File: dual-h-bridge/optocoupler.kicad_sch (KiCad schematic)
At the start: 5 parts, among them U2 MCT6

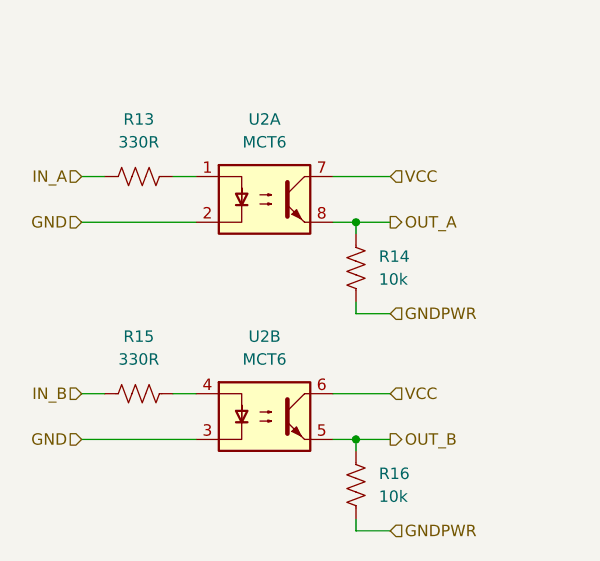
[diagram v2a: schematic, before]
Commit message: Fix optocoupler hardware issue
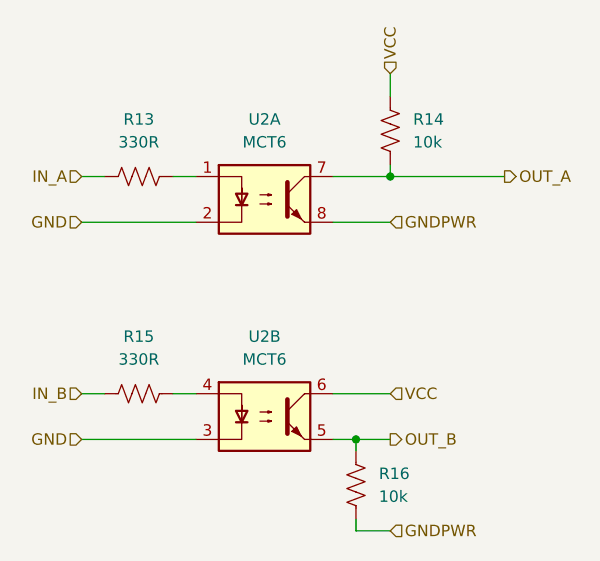
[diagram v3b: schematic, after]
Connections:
- net GNDPWR: now also U2.8; no longer R14.1
- net OUT_A: now also R14.1, U2.7; no longer R14.2, U2.8
- net VCC: now also R14.2; no longer U2.7
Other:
- moved on the sheet: R14
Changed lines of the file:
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@@
 	(title_block
 		(title "Optocoupler")
-		(date "2025-07-06")
-		(rev "v2.0.1")
+		(date "2025-07-09")
+		(rev "v3.0.0")
 		(company "Team 5")
 		(comment 1 "George Sleen")
 	)
 	(junction
-		(at 115.57 54.61)
+		(at 119.38 49.53)
 		(diameter 0)
 		(color 0 0 0 0)
@@
 	(wire
 		(pts
-			(xy 115.57 54.61) (xy 113.03 54.61)
+			(xy 113.03 54.61) (xy 119.38 54.61)
 		)
 		(stroke
@@
 	(wire
 		(pts
-			(xy 115.57 63.5) (xy 115.57 64.77)
-		)
-		(stroke
-			(width 0)
-			(type default)
-		)
-	)
-	(wire
-		(pts
 			(xy 115.57 78.74) (xy 113.03 78.74)
 		)
@@
 	(wire
 		(pts
+			(xy 132.08 49.53) (xy 119.38 49.53)
+		)
+		(stroke
+			(width 0)
+			(type default)
+		)
+	)
+	(wire
+		(pts
+			(xy 119.38 38.1) (xy 119.38 40.64)
+		)
+		(stroke
+			(width 0)
+			(type default)
+		)
+	)
+	(wire
+		(pts
 			(xy 87.63 73.66) (xy 85.09 73.66)
 		)
@@
 	(wire
 		(pts
-			(xy 113.03 49.53) (xy 119.38 49.53)
+			(xy 119.38 49.53) (xy 113.03 49.53)
 		)
 		(stroke
@@
 	(wire
 		(pts
-			(xy 115.57 55.88) (xy 115.57 54.61)
-		)
-		(stroke
-			(width 0)
-			(type default)
-		)
-	)
-	(wire
-		(pts
-			(xy 115.57 54.61) (xy 119.38 54.61)
+			(xy 119.38 48.26) (xy 119.38 49.53)
 		)
 		(stroke
@@
 		)
 	)
-	(wire
-		(pts
-			(xy 115.57 64.77) (xy 119.38 64.77)
-		)
-		(stroke
-			(width 0)
-			(type default)
-		)
-	)
 	(hierarchical_label "VCC"
 		(shape input)
-		(at 119.38 49.53 0)
+		(at 119.38 38.1 90)
 		(effects
 			(font
@@
 	(hierarchical_label "OUT_A"
 		(shape output)
-		(at 119.38 54.61 0)
+		(at 132.08 49.53 0)
 		(effects
 			(font
@@
 	(hierarchical_label "GNDPWR"
 		(shape input)
-		(at 119.38 64.77 0)
+		(at 119.38 54.61 0)
 		(effects
 			(font
@@
 	(symbol
 		(lib_id "Device:R_US")
-		(at 115.57 59.69 180)
+		(at 119.38 44.45 180)
 		(unit 1)
 		(exclude_from_sim no)
@@
 		(fields_autoplaced yes)
 		(property "Reference" "R14"
-			(at 118.11 58.4199 0)
+			(at 121.92 43.1799 0)
 			(effects
 				(font
@@
 		)
 		(property "Value" "10k"
-			(at 118.11 60.9599 0)
+			(at 121.92 45.7199 0)
 			(effects
 				(font
@@
 		)
 		(property "Footprint" "Resistor_THT:R_Axial_DIN0309_L9.0mm_D3.2mm_P12.70mm_Horizontal"
-			(at 114.554 59.436 90)
+			(at 118.364 44.196 90)
 			(effects
 				(font
@@
 		)
 		(property "Datasheet" "~"
-			(at 115.57 59.69 0)
+			(at 119.38 44.45 0)
 			(effects
 				(font
@@
 		)
 		(property "Description" "Resistor, US symbol"
-			(at 115.57 59.69 0)
-			(effects
-				(font
+			(at 119.38 44.45 0)
+			(effects
+				(font

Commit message: More changes
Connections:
- net GNDPWR: now also U2.5; no longer R16.1
- net OUT_B: now also R16.1, U2.6; no longer R16.2, U2.5
- net VCC: now also R16.2; no longer U2.6
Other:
- moved on the sheet: R16
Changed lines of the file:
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@@
+	)
+	(junction
+		(at 119.38 73.66)
+		(diameter 0)
+		(color 0 0 0 0)
 	)
 	(junction
@@
 		(color 0 0 0 0)
 	)
-	(junction
-		(at 115.57 78.74)
-		(diameter 0)
-		(color 0 0 0 0)
-	)
 	(wire
 		(pts
@@
 	(wire
 		(pts
-			(xy 115.57 78.74) (xy 113.03 78.74)
-		)
-		(stroke
-			(width 0)
-			(type default)
-		)
-	)
-	(wire
-		(pts
-			(xy 115.57 80.01) (xy 115.57 78.74)
+			(xy 113.03 73.66) (xy 119.38 73.66)
+		)
+		(stroke
+			(width 0)
+			(type default)
+		)
+	)
+	(wire
+		(pts
+			(xy 113.03 78.74) (xy 119.38 78.74)
 		)
 		(stroke
@@
 	(wire
 		(pts
-			(xy 119.38 38.1) (xy 119.38 40.64)
-		)
-		(stroke
-			(width 0)
-			(type default)
-		)
-	)
-	(wire
-		(pts
 			(xy 87.63 73.66) (xy 85.09 73.66)
 		)
@@
 	(wire
 		(pts
+			(xy 119.38 72.39) (xy 119.38 73.66)
+		)
+		(stroke
+			(width 0)
+			(type default)
+		)
+	)
+	(wire
+		(pts
 			(xy 85.09 54.61) (xy 97.79 54.61)
 		)
@@
 	(wire
 		(pts
-			(xy 115.57 87.63) (xy 115.57 88.9)
-		)
-		(stroke
-			(width 0)
-			(type default)
-		)
-	)
-	(wire
-		(pts
 			(xy 119.38 49.53) (xy 113.03 49.53)
 		)
@@
 	(wire
 		(pts
-			(xy 115.57 88.9) (xy 119.38 88.9)
+			(xy 119.38 73.66) (xy 132.08 73.66)
 		)
 		(stroke
@@
 	(wire
 		(pts
-			(xy 113.03 73.66) (xy 119.38 73.66)
-		)
-		(stroke
-			(width 0)
-			(type default)
-		)
-	)
-	(wire
-		(pts
 			(xy 85.09 78.74) (xy 97.79 78.74)
 		)
@@
 		)
 	)
-	(wire
-		(pts
-			(xy 119.38 78.74) (xy 115.57 78.74)
-		)
-		(stroke
-			(width 0)
-			(type default)
-		)
-	)
 	(hierarchical_label "VCC"
 		(shape input)
-		(at 119.38 38.1 90)
+		(at 119.38 40.64 90)
+		(effects
+			(font
+				(size 1.27 1.27)
+			)
+			(justify left)
+		)
+	)
+	(hierarchical_label "OUT_B"
+		(shape output)
+		(at 132.08 73.66 0)
 		(effects
 			(font
@@
 		)
 	)
-	(hierarchical_label "OUT_B"
-		(shape output)
+	(hierarchical_label "GNDPWR"
+		(shape input)
 		(at 119.38 78.74 0)
 		(effects
@@
 	(hierarchical_label "GNDPWR"
 		(shape input)
-		(at 119.38 88.9 0)
+		(at 119.38 54.61 0)
 		(effects
 			(font
@@
 		)
 	)
-	(hierarchical_label "GNDPWR"
-		(shape input)
-		(at 119.38 54.61 0)
-		(effects
-			(font
-				(size 1.27 1.27)
-			)
-			(justify left)
-		)
-	)
 	(hierarchical_label "GND"
 		(shape input)
@@
 	(hierarchical_label "VCC"
 		(shape input)
-		(at 119.38 73.66 0)
+		(at 119.38 64.77 90)
 		(effects
 			(font
@@
 	(symbol
 		(lib_id "Device:R_US")
-		(at 115.57 83.82 180)
+		(at 119.38 68.58 180)
 		(unit 1)
 		(exclude_from_sim no)
@@
 		(fields_autoplaced yes)
 		(property "Reference" "R16"
-			(at 118.11 82.5499 0)
+			(at 121.92 67.3099 0)
 			(effects
 				(font
@@
 		)
 		(property "Value" "10k"
-			(at 118.11 85.0899 0)
+			(at 121.92 69.8499 0)
 			(effects
 				(font
@@
 		)
 		(property "Footprint" "Resistor_THT:R_Axial_DIN0309_L9.0mm_D3.2mm_P12.70mm_Horizontal"
-			(at 114.554 83.566 90)
+			(at 118.364 68.326 90)
 			(effects
 				(font
@@
 		)
 		(property "Datasheet" "~"
-			(at 115.57 83.82 0)
+			(at 119.38 68.58 0)
 			(effects
 				(font
@@
 		)
 		(property "Description" "Resistor, US symbol"
-			(at 115.57 83.82 0)
+			(at 119.38 68.58 0)
 			(effects
 				(font
@@
 		)
 		(instances
-			(project "motor-controller"
+			(project "dual-h-bridge"
 				(path "/3cf627b4-179f-4b19-ad57-a5207e12b14c/8df6f006-2f8a-45b2-b2f5-cd2a57657185"
-					(reference "R20")
+					(reference "R16")
 					(unit 1)
 				)

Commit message: Fix all hardware issues and generate final release source files
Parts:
- renumbered R14 to R13, R13 to R14, R16 to R15, R15 to R16
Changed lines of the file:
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@@
 		(dnp no)
 		(fields_autoplaced yes)
-		(property "Reference" "R14"
+		(property "Reference" "R13"
 			(at 121.92 43.1799 0)
 			(effects
@@
 			(project "motor-controller"
 				(path "/3cf627b4-179f-4b19-ad57-a5207e12b14c/8df6f006-2f8a-45b2-b2f5-cd2a57657185"
-					(reference "R18")
-					(unit 1)
-				)
-				(path "/3cf627b4-179f-4b19-ad57-a5207e12b14c/b71eba93-a5ac-44ab-8657-fb36dfe25929"
-					(reference "R14")
+					(reference "R17")
+					(unit 1)
+				)
+				(path "/3cf627b4-179f-4b19-ad57-a5207e12b14c/b71eba93-a5ac-44ab-8657-fb36dfe25929"
+					(reference "R13")
 					(unit 1)
 				)
@@
 		(dnp no)
 		(fields_autoplaced yes)
-		(property "Reference" "R16"
+		(property "Reference" "R15"
 			(at 121.92 67.3099 0)
 			(effects
@@
 			(project "dual-h-bridge"
 				(path "/3cf627b4-179f-4b19-ad57-a5207e12b14c/8df6f006-2f8a-45b2-b2f5-cd2a57657185"
-					(reference "R16")
-					(unit 1)
-				)
-				(path "/3cf627b4-179f-4b19-ad57-a5207e12b14c/b71eba93-a5ac-44ab-8657-fb36dfe25929"
-					(reference "R16")
+					(reference "R19")
+					(unit 1)
+				)
+				(path "/3cf627b4-179f-4b19-ad57-a5207e12b14c/b71eba93-a5ac-44ab-8657-fb36dfe25929"
+					(reference "R15")
 					(unit 1)
 				)
@@
 		(dnp no)
 		(fields_autoplaced yes)
-		(property "Reference" "R13"
+		(property "Reference" "R14"
 			(at 91.44 43.18 90)
 			(effects
@@
 			(project "motor-controller"
 				(path "/3cf627b4-179f-4b19-ad57-a5207e12b14c/8df6f006-2f8a-45b2-b2f5-cd2a57657185"
-					(reference "R17")
-					(unit 1)
-				)
-				(path "/3cf627b4-179f-4b19-ad57-a5207e12b14c/b71eba93-a5ac-44ab-8657-fb36dfe25929"
-					(reference "R13")
+					(reference "R18")
+					(unit 1)
+				)
+				(path "/3cf627b4-179f-4b19-ad57-a5207e12b14c/b71eba93-a5ac-44ab-8657-fb36dfe25929"
+					(reference "R14")
 					(unit 1)
 				)
@@
 		(dnp no)
 		(fields_autoplaced yes)
-		(property "Reference" "R15"
+		(property "Reference" "R16"
 			(at 91.44 67.31 90)
 			(effects
@@
 			(project "motor-controller"
 				(path "/3cf627b4-179f-4b19-ad57-a5207e12b14c/8df6f006-2f8a-45b2-b2f5-cd2a57657185"
-					(reference "R19")
-					(unit 1)
-				)
-				(path "/3cf627b4-179f-4b19-ad57-a5207e12b14c/b71eba93-a5ac-44ab-8657-fb36dfe25929"
-					(reference "R15")
-					(unit 1)
-				)
+					(reference "R20")
+					(unit 1)
+				)
+				(path "/3cf627b4-179f-4b19-ad57-a5207e12b14c/b71eba93-a5ac-44ab-8657-fb36dfe25929"
+					(reference "R16")
+					(unit 1)
+				)
